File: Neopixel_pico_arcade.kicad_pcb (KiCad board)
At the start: 4 copper layers, 100 x 88 mm, 147 parts, among them J1 SWD_connector, J2 NES_controller_connector, J3 USB_C_Receptacle_USB2.0, Q1 2N7002, U1 RP2040_Stamp, U2 SN74LV1T34DBV, U3 SRV05-4HTG-D

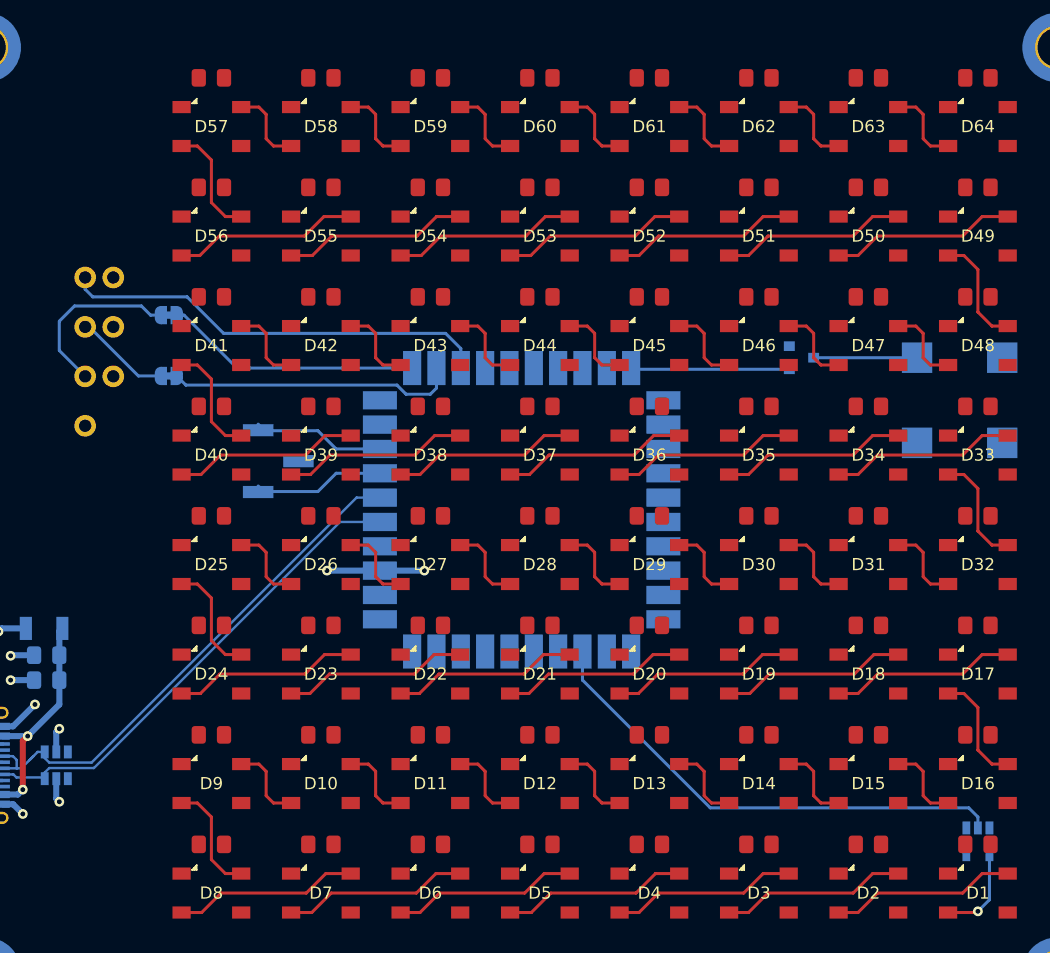
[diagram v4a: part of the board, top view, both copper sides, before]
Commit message: Routes ground for LEDs and their decoupling capacitors
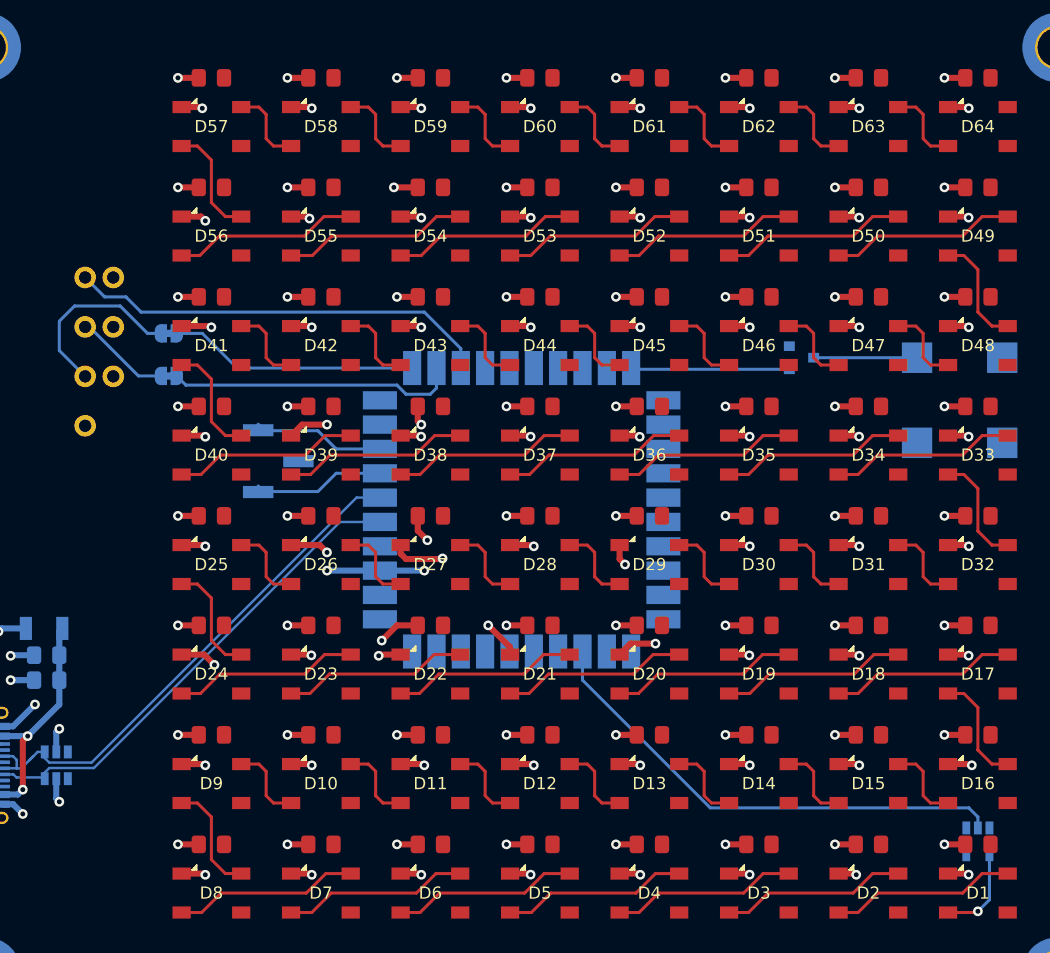
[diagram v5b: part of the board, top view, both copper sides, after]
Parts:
- moved JP1 1.50 mm to (121.0, 79.5)
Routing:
- net GND: track 11.2 -> 247.2 mm, vias 5 -> 133
- net Net-(J2-Pad2): track 14.6 -> 15.2 mm
- net CTRL_CLK: track 21.2 -> 20.5 mm
- net CTRL_DATA: track 35.5 -> 34.9 mm

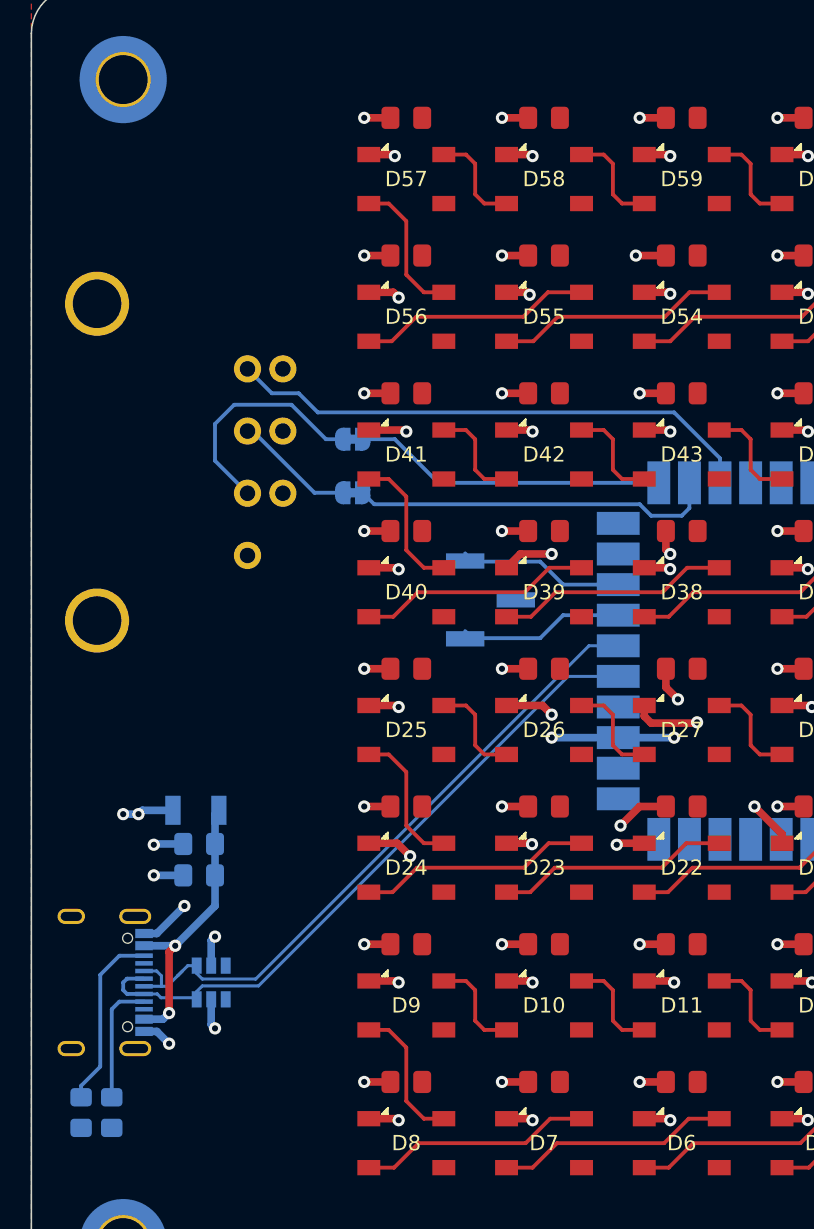
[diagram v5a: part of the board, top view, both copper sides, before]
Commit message: Changes positions of the controller and USB connector
This makes it easier to route the USB signal and also makes more sense
since the NES connector and cable are pretty heavy and will probably be
better bellow.
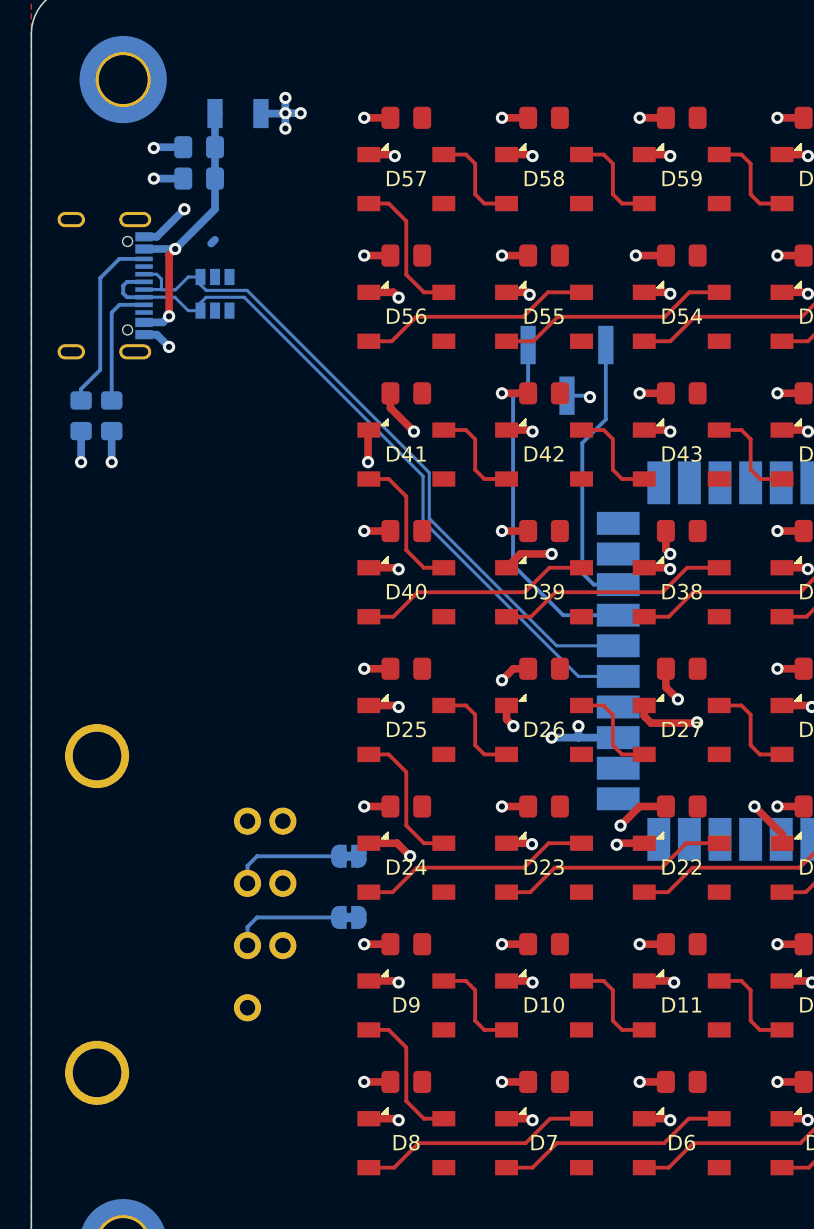
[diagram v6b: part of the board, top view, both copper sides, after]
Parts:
- moved F1 45.6 mm to (113.5, 58.2), turned to 0 degrees
- moved C1 45.5 mm to (111.0, 62.5)
- moved C2 45.5 mm to (111.0, 60.4)
- moved J3 45.5 mm to (105.0, 69.5)
- moved R1 45.5 mm to (105.2, 78.0)
- moved R2 45.5 mm to (103.2, 78.0)
- moved U3 45.0 mm to (112.0, 70.0)
- moved JP1 31.3 mm to (120.8, 110.8)
- moved J2 29.6 mm to (115.3, 110.6)
- moved JP2 23.8 mm to (120.8, 106.8)
- moved J1 15.8 mm to (135.0, 75.0), turned to -90 degrees
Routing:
- net CTRL_DATA: track 34.9 -> 0.00 mm
- net CTRL_LATCH: track 23.8 -> 0.00 mm
- net CTRL_CLK: track 20.5 -> 0.00 mm
- net SWDIO: track 10.8 -> 23.0 mm
- net Net-(J2-Pad2): track 15.2 -> 7.45 mm
- net SWCLK: track 10.8 -> 18.2 mm
- net USB_D-: track 43.6 -> 47.4 mm
- net GND: track 247.2 -> 250.9 mm, vias 133 -> 135
- net +5V: track 13.4 -> 9.71 mm, vias 5 -> 6
- net USB_D+: track 43.6 -> 45.3 mm
- net Net-(J2-Pad3): track 7.90 -> 7.38 mm

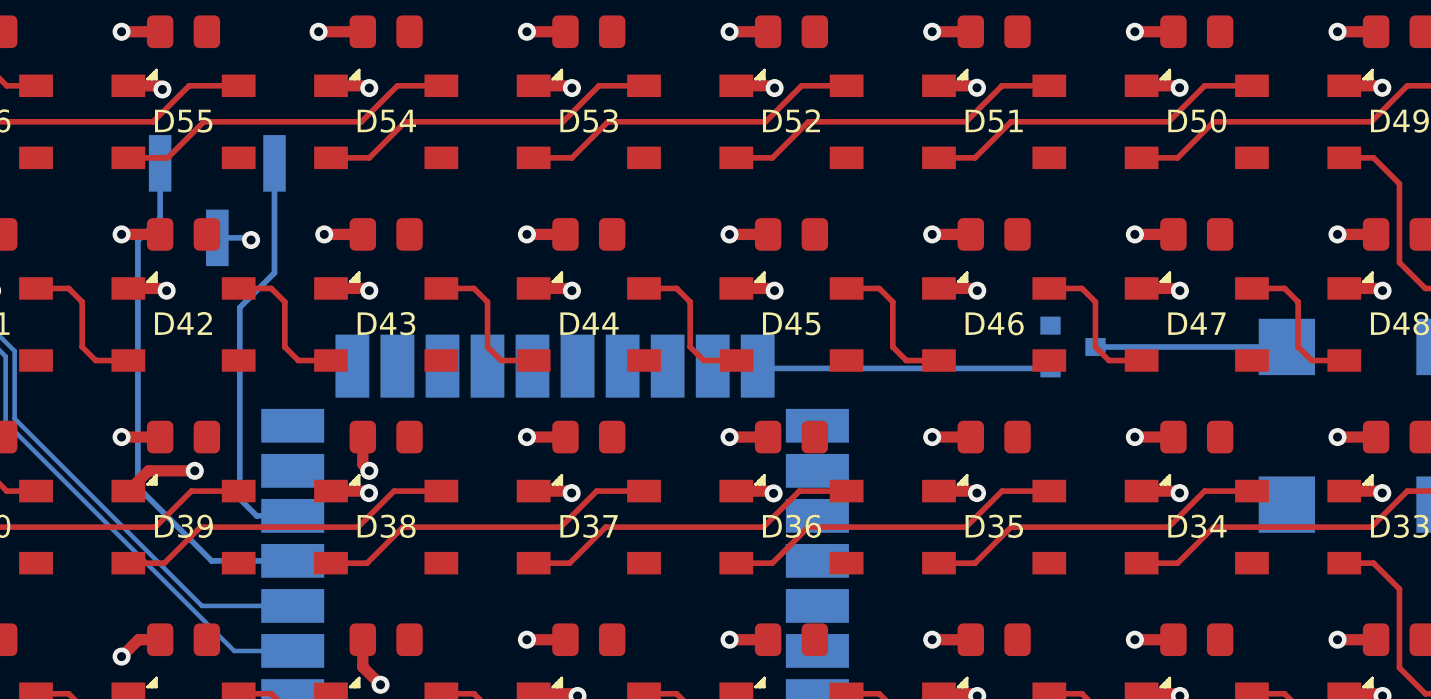
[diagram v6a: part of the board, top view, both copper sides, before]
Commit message: Removes SWD header
We will very likely not need it anyways since we have a USB connection
for programming.
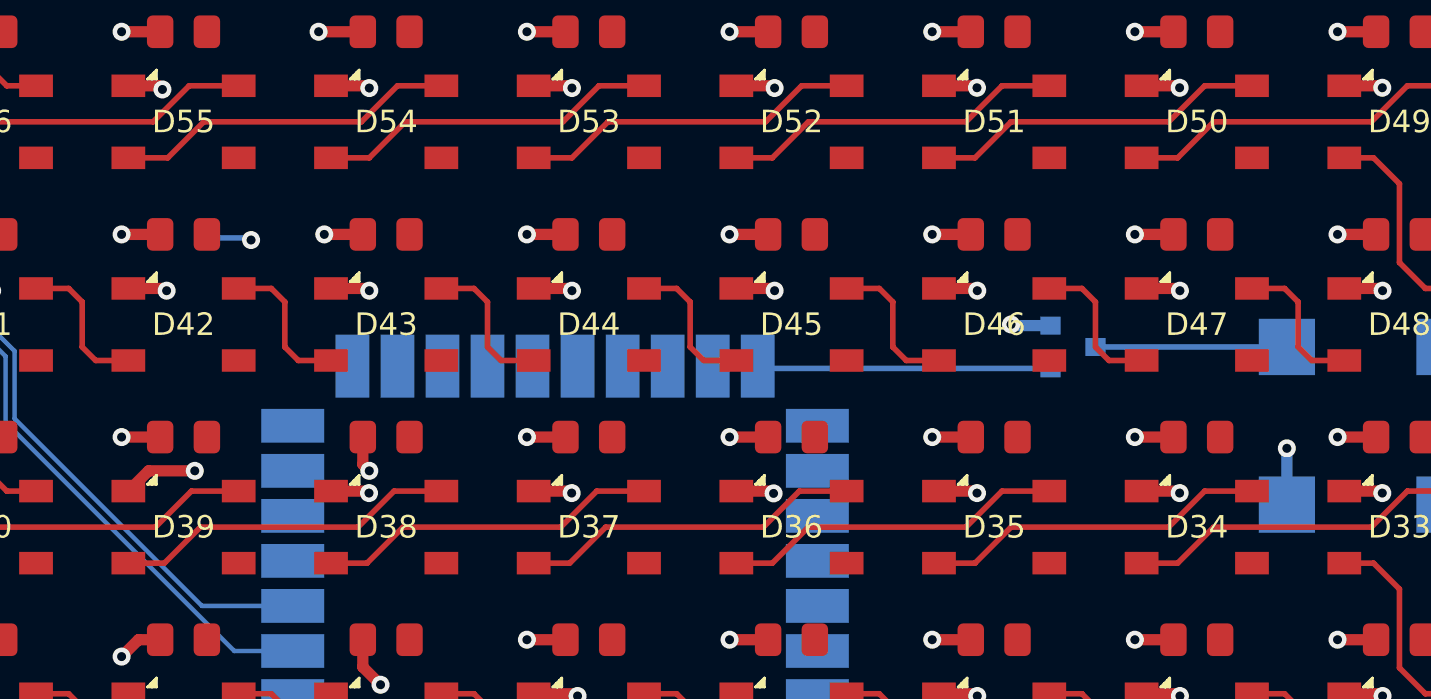
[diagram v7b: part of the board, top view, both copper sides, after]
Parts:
- removed J1: SWD_connector, Connector_PinHeader_2.54mm:PinHeader_1x03_P2.54mm_Vertical_SMD_Pin1Left
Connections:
- U1 pad 37: SWDIO -> unconnected-(U1-Pad37)
- U1 pad 38: SWCLK -> unconnected-(U1-Pad38)
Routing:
- net SWDIO: track 23.0 -> 0.00 mm
- net SWCLK: track 18.2 -> 0.00 mm
- net +5V: track 9.71 -> 12.2 mm, vias 6 -> 7
- net GND: track 250.9 -> 252.7 mm, vias 135 -> 136

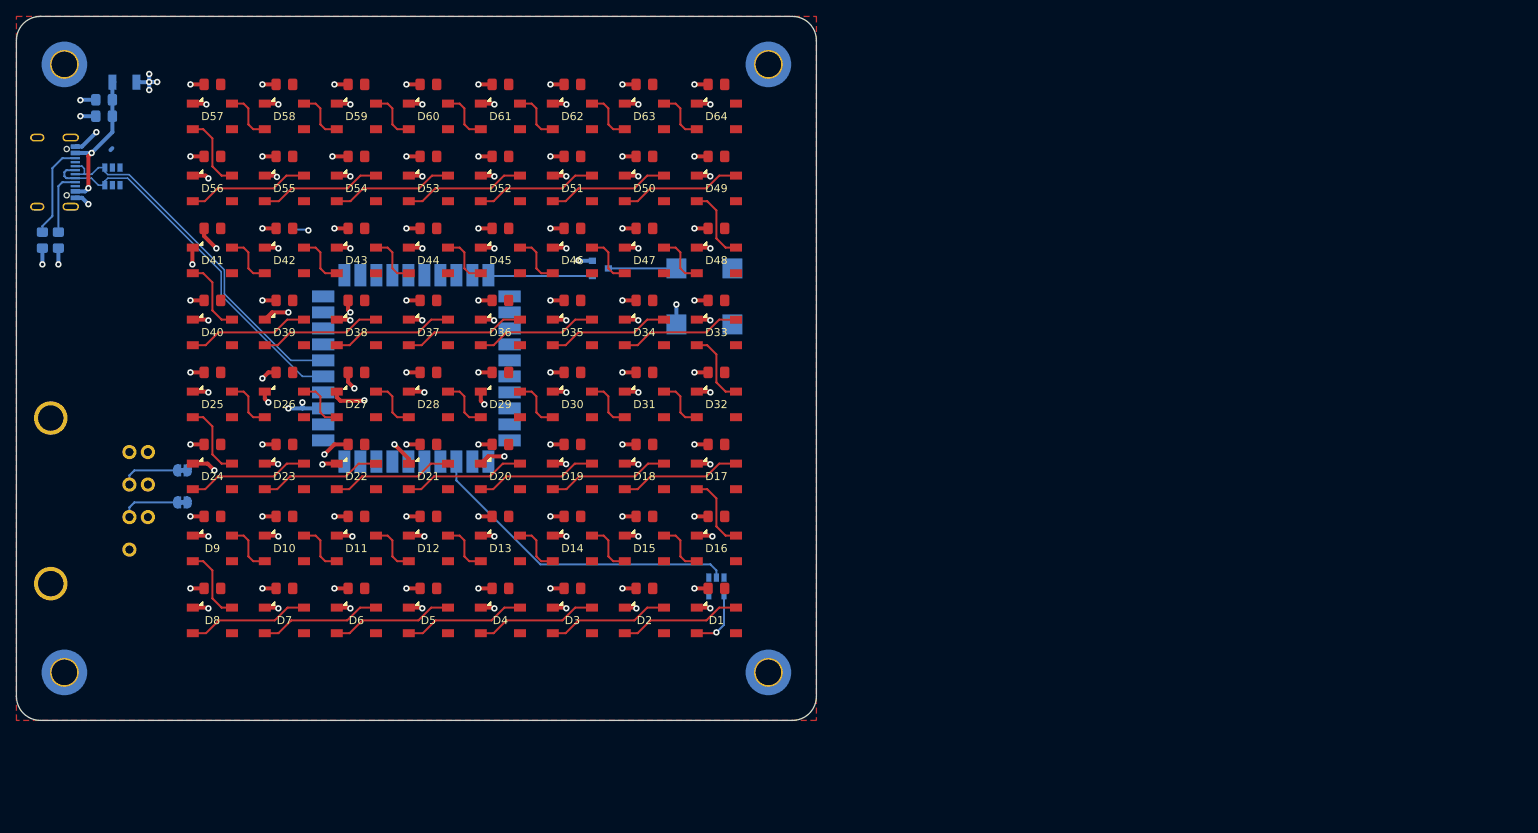
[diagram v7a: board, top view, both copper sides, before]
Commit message: Reroutes NES controler lines
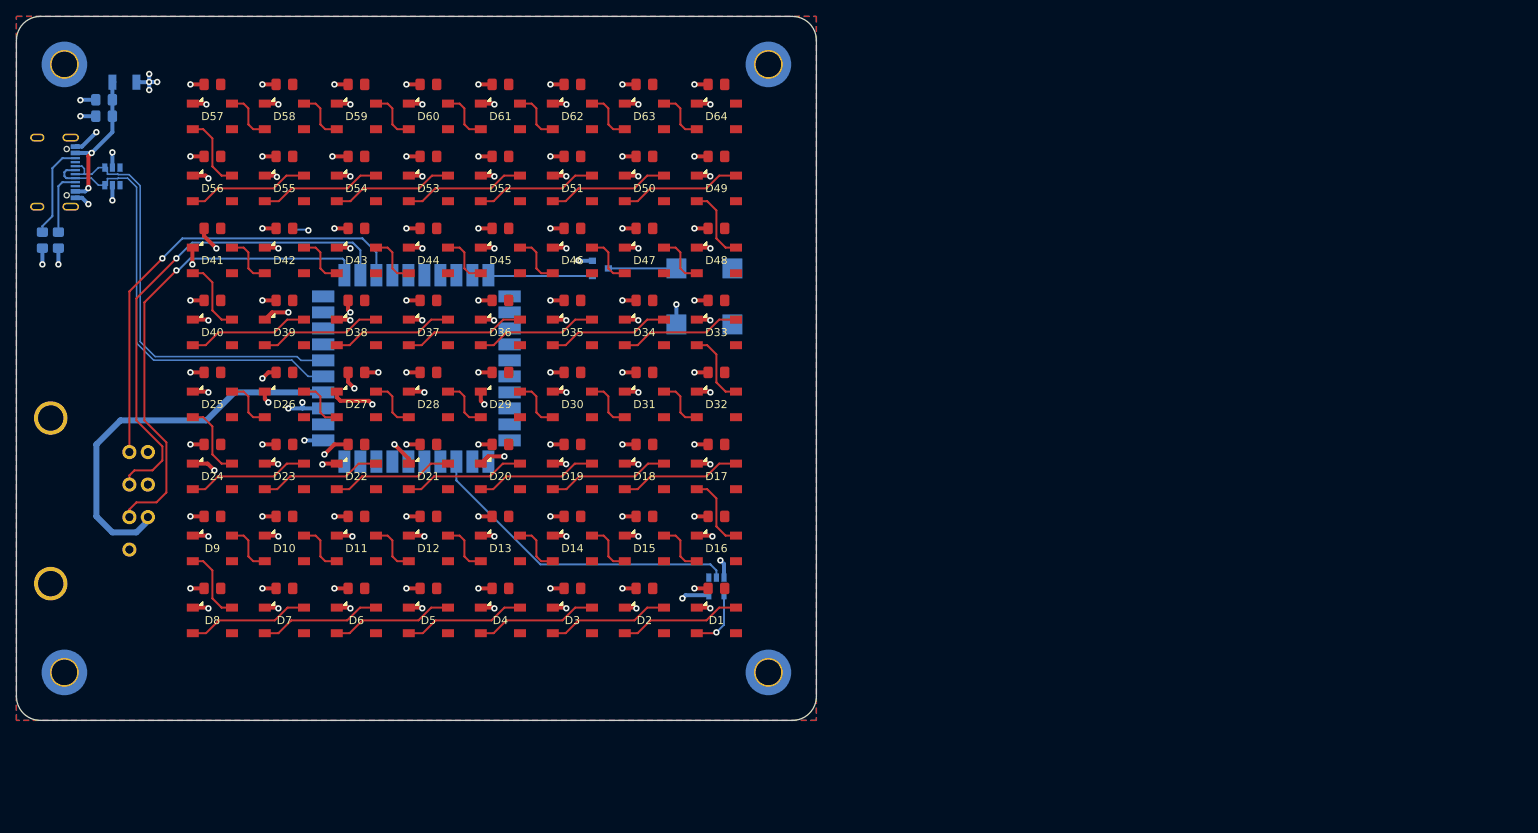
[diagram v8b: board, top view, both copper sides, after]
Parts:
- removed JP1, JP2: jmp, Jumper:SolderJumper-2_P1.3mm_Bridged_RoundedPad1.0x1.5mm
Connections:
- J2 pad 2: Net-(J2-Pad2) -> CTRL_CLK
- J2 pad 3: Net-(J2-Pad3) -> CTRL_LATCH
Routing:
- net CTRL_LATCH: track 0.00 -> 62.1 mm, vias 0 -> 1
- net CTRL_CLK: track 0.00 -> 61.1 mm, vias 0 -> 1
- net CTRL_DATA: track 0.00 -> 57.3 mm, vias 0 -> 1
- net +3V3: track 0.00 -> 48.4 mm
- net USB_D-: track 47.4 -> 57.3 mm
- net USB_D+: track 45.3 -> 55.2 mm
- net Net-(J2-Pad2): track 7.45 -> 0.00 mm
- net GND: track 252.7 -> 260.1 mm, vias 136 -> 139
- net Net-(J2-Pad3): track 7.38 -> 0.00 mm
- net +5V: track 12.2 -> 19.3 mm, vias 7 -> 10
- added copper zone on B.Cu, net +5V
